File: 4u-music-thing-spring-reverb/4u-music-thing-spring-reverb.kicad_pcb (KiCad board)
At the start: 2 copper layers, 52.8 x 111.5 mm, 52 parts, among them J1 IN1, J2 IN2, J4 OUT, J5 Conn_01x04_Male, J7 CTRL_BOARD_HEADER, J8 MAIN_BOARD_HEADER, U1 TL072, U2 NE5532

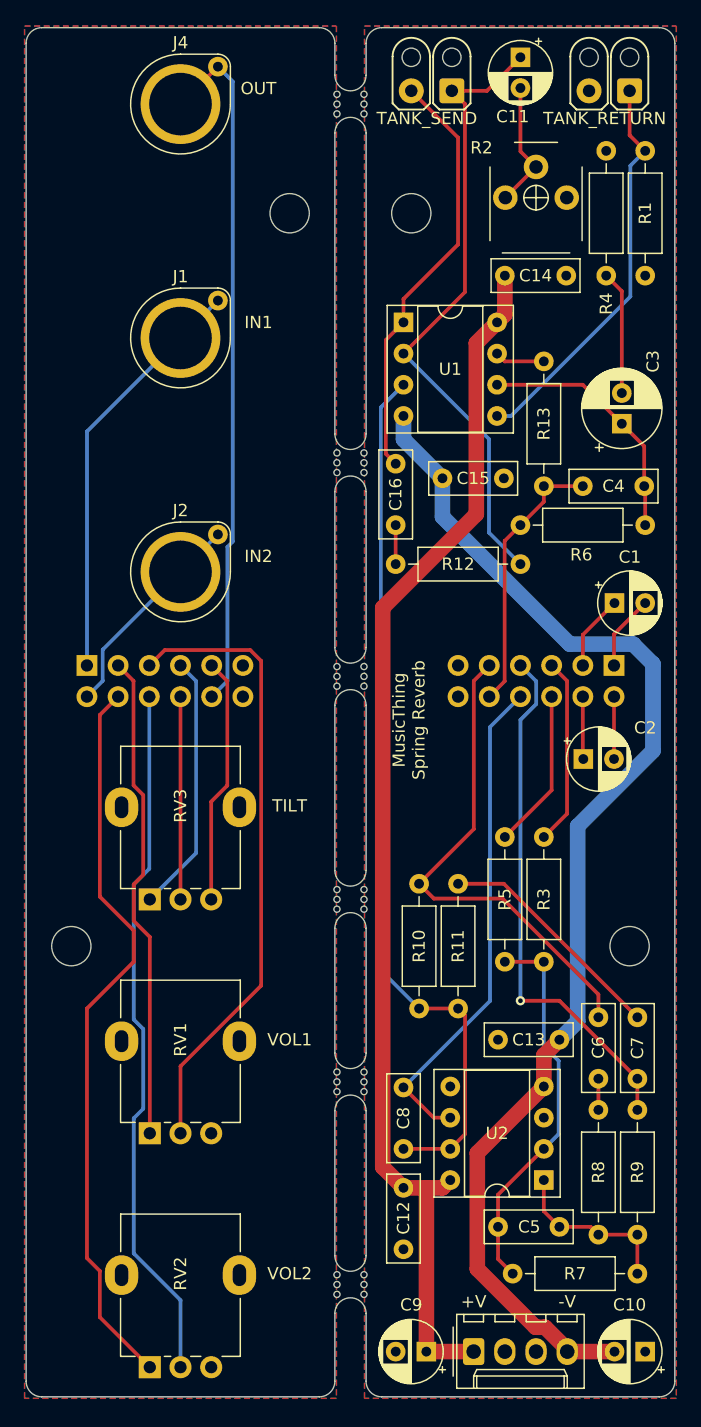
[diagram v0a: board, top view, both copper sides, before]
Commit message: Updated version of music thing spring reverb
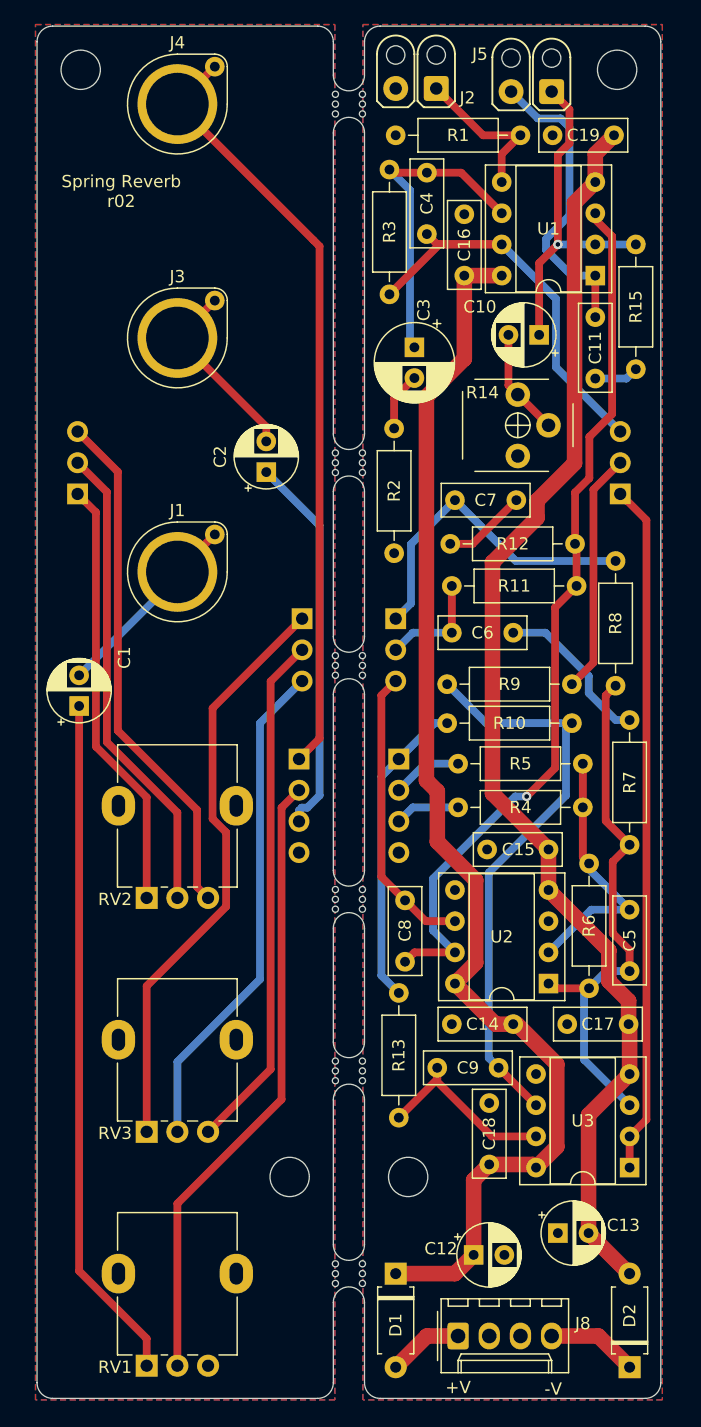
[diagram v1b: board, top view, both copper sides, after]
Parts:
- removed the REF** at (120.9, 53.3)
- removed the REF** at (130.8, 53.3)
- removed the REF** at (148.6, 113.0)
- removed the REF** at (103.1, 113.0)
- removed TANK_RETURN: REV_RETURN, rumblesan-footprints:SolderWire-24AWG-0.2sqmm_1x02_D0.5mm_OD1.1mm_Relief
- removed TANK_SEND: REV_SEND, rumblesan-footprints:SolderWire-24AWG-0.2sqmm_1x02_D0.5mm_OD1.1mm_Relief
- added C17: 100nf, Capacitor_THT:C_Rect_L7.0mm_W2.5mm_P5.00mm, F.Cu at (143.5, 119.4)
- added C18: 100nf, Capacitor_THT:C_Rect_L7.0mm_W2.5mm_P5.00mm, F.Cu at (137.2, 130.8)
- added C19: 100nf, Capacitor_THT:C_Rect_L7.0mm_W2.5mm_P5.00mm, F.Cu at (142.3, 47.0)
- added D1: D, rumblesan-footprints:Diode_THT_P7.62mm_Horizontal, F.Cu at (129.5, 139.7)
- added D2: D, rumblesan-footprints:Diode_THT_P7.62mm_Horizontal, F.Cu at (148.6, 147.3)
- added J10: MIX_MAIN, Connector_PinSocket_2.54mm:PinSocket_1x03_P2.54mm_Vertical, B.Cu at (147.8, 76.2)
- added J11: AUDIO_IO_MAIN, Connector_PinSocket_2.54mm:PinSocket_1x04_P2.54mm_Vertical, B.Cu at (129.8, 97.8)
- added J12: AUDIO_IO_CTRL, Connector_PinHeader_2.54mm:PinHeader_1x04_P2.54mm_Vertical, B.Cu at (121.7, 97.8)
- added J3: IN2, rumblesan-footprints:BananaJack_THT_JohnsonCinch_108-09, F.Cu at (111.8, 63.5)
- added J6: TILT_MAIN, Connector_PinSocket_2.54mm:PinSocket_1x03_P2.54mm_Vertical, B.Cu at (129.5, 86.4)
- added J9: MIX_CTRL, Connector_PinHeader_2.54mm:PinHeader_1x03_P2.54mm_Vertical, B.Cu at (103.6, 76.2)
- added R14: 10k, rumblesan-footprints:Potentiometer_THT_Bourns_3306P_Vertical, F.Cu at (139.5, 70.6)
- added R15: 2k2, rumblesan-footprints:Resistor_THT_L6.3mm_D2.5mm_P10.16mm_Horizontal, F.Cu at (149.1, 66.0)
- added REF**: MountingHole_3.2mm_M3, MountingHole:MountingHole_3.2mm_M3, F.Cu at (103.9, 41.7)
- added REF**: MountingHole_3.2mm_M3, MountingHole:MountingHole_3.2mm_M3, F.Cu at (130.6, 131.8)
- added REF**: MountingHole_3.2mm_M3, MountingHole:MountingHole_3.2mm_M3, F.Cu at (120.9, 131.8)
- added REF**: MountingHole_3.2mm_M3, MountingHole:MountingHole_3.2mm_M3, F.Cu at (147.6, 41.7)
- added U3: TL072, Package_DIP:DIP-8_W7.62mm_Socket, F.Cu at (148.6, 131.1)
- C11: value 10uf -> 10nf; footprint Capacitor_THT:CP_Radial_D5.0mm_P2.50mm -> Capacitor_THT:C_Rect_L7.0mm_W2.5mm_P5.00mm
- C12, C13: value 100nf -> 10uf; footprint Capacitor_THT:C_Rect_L7.0mm_W2.5mm_P5.00mm -> Capacitor_THT:CP_Radial_D5.0mm_P2.50mm
- C16: value 10nf -> 100nf
- C9: value 10uf -> 22pf; footprint Capacitor_THT:CP_Radial_D5.0mm_P2.50mm -> Capacitor_THT:C_Rect_L7.0mm_W2.5mm_P5.00mm
- J2: value IN2 -> REV_RETURN; footprint rumblesan-footprints:BananaJack_THT_JohnsonCinch_108-09 -> rumblesan-footprints:SolderWire-24AWG-0.2sqmm_1x02_D0.5mm_OD1.1mm_Relief
- J5: value Conn_01x04_Male -> REV_SEND; footprint rumblesan-footprints:Molex_KK-254_AE-6410-04A_1x04_P2.54mm_Vertical -> rumblesan-footprints:SolderWire-24AWG-0.2sqmm_1x02_D0.5mm_OD1.1mm_Relief
- J7: value CTRL_BOARD_HEADER -> TILT_CTRL; footprint Connector_PinHeader_2.54mm:PinHeader_2x06_P2.54mm_Vertical -> Connector_PinHeader_2.54mm:PinHeader_1x03_P2.54mm_Vertical
- J8: value MAIN_BOARD_HEADER -> Conn_01x04_Male; footprint Connector_PinSocket_2.54mm:PinSocket_2x06_P2.54mm_Vertical -> rumblesan-footprints:Molex_KK-254_AE-6410-04A_1x04_P2.54mm_Vertical; moved to F.Cu
- R10, R9: value 6k8 -> 100k
- R11, R8: value 2k2 -> 6k8
- R13: value 1k -> 330
- R2: value 10k -> 22r; footprint rumblesan-footprints:Potentiometer_THT_Bourns_3306P_Vertical -> rumblesan-footprints:Resistor_THT_L6.3mm_D2.5mm_P10.16mm_Horizontal
- R3: value 10k -> 22k
- R4: value 22r -> 10k
- R6: value 22k -> 10k
- R7: value 10k -> 2k2
- moved J5 102.8 mm to (142.2, 43.4), turned to 180 degrees
- moved C10 83.3 mm to (141.2, 63.2)
- moved C14 61.0 mm to (139.1, 119.4), turned to 180 degrees
- moved J8 56.1 mm to (134.6, 144.8), turned to 0 degrees
- moved R3 55.8 mm to (129.0, 59.9)
- moved RV2 45.8 mm to (111.8, 101.6)
- moved R7 45.1 mm to (148.6, 94.6), turned to 270 degrees
- moved R8 44.7 mm to (147.4, 81.7)
- moved J2 44.5 mm to (132.8, 43.2), turned to 180 degrees
- moved C1 44.4 mm to (103.8, 93.5), turned to 90 degrees
- moved R4 43.3 mm to (144.8, 101.7), turned to 180 degrees
- moved C7 43.3 mm to (139.4, 76.7), turned to 180 degrees
- moved R13 42.9 mm to (129.8, 116.8), turned to 270 degrees
- moved R6 38.1 mm to (145.3, 116.5), turned to 90 degrees
- moved R9 38.0 mm to (133.7, 91.7), turned to 0 degrees
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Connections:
- C1 pad 1: /AUDIO1_VOL_MAIN -> Net-(C1-Pad1)
- C1 pad 2: /AUDIO1_IN_MAIN -> Net-(C1-Pad2)
- C10 pad 1: GND -> Net-(C10-Pad1)
- C10 pad 2: -12V -> Net-(C10-Pad2)
- C16 pad 1: Net-(C16-Pad1) -> +12V
- C16 pad 2: Net-(C16-Pad2) -> GND
- C2 pad 1: /AUDIO2_VOL_MAIN -> /AUDIO2_IN_CTRL
- C2 pad 2: /AUDIO2_IN_MAIN -> Net-(C2-Pad2)
- C4 pad 1: /AUDIO_OUT_MAIN -> /AUDIO_WET_MAIN
- C5 pad 1: Net-(C5-Pad1) -> /AUDIO_MIX
- C9 pad 1: +12V -> Net-(C9-Pad1)
- C9 pad 2: GND -> Net-(C9-Pad2)
- J1 pad 1: /AUDIO1_IN_CTRL -> Net-(C1-Pad2)
- J2 pad 1: /AUDIO2_IN_CTRL -> Net-(J2-Pad1)
- J5 pad 1: +12V -> Net-(C10-Pad1)
- J5 pad 2: GND -> Net-(C11-Pad1)
- J7 pad 1: /AUDIO1_IN_CTRL -> /TILT_LO_CTRL
- J7 pad 2: /AUDIO2_IN_CTRL -> /TILT_HI_CTRL
- J7 pad 3: /AUDIO1_VOL_CTRL -> /TILT_CENTRE_CTRL
- J8 pad 1: /AUDIO1_IN_MAIN -> Net-(D1-Pad2)
- J8 pad 2: /AUDIO2_IN_MAIN -> GND
- J8 pad 3: /AUDIO1_VOL_MAIN -> GND
- J8 pad 4: /AUDIO2_VOL_MAIN -> Net-(D2-Pad1)
- R1 pad 1: Net-(J3-Pad1) -> Net-(J2-Pad1)
- R10 pad 1: Net-(C8-Pad1) -> /AUDIO_OUT_MAIN
- R10 pad 2: /TILT_HI_MAIN -> Net-(C9-Pad2)
- R11 pad 2: Net-(C7-Pad1) -> /TILT_HI_MAIN
- R12 pad 1: Net-(C16-Pad2) -> Net-(C8-Pad1)
- R12 pad 2: Net-(C11-Pad1) -> Net-(C7-Pad1)
- R13 pad 2: Net-(R13-Pad2) -> Net-(C9-Pad1)
- R2 pad 1: Net-(C11-Pad2) -> Net-(C3-Pad2)
- R2 pad 2: Net-(C11-Pad2) -> GND
- R3 pad 1: Net-(C5-Pad2) -> /AUDIO_WET_MAIN
- R3 pad 2: /AUDIO1_POST_VOL_MAIN -> Net-(C3-Pad1)
- R4 pad 1: Net-(C3-Pad2) -> Net-(C5-Pad2)
- R4 pad 2: GND -> /AUDIO2_IN_MAIN
- R5 pad 2: /AUDIO2_POST_VOL_MAIN -> /AUDIO1_IN_MAIN
- R6 pad 1: /AUDIO_OUT_MAIN -> /AUDIO_MIX
- R6 pad 2: Net-(C3-Pad1) -> Net-(C5-Pad2)
- R7 pad 1: Net-(C5-Pad1) -> Net-(C6-Pad2)
- R7 pad 2: Net-(C5-Pad2) -> /AUDIO_MIX
- R8 pad 1: Net-(C6-Pad2) -> /TILT_LO_MAIN
- R8 pad 2: Net-(C5-Pad1) -> /AUDIO_MIX
- R9 pad 1: /TILT_LO_MAIN -> Net-(C9-Pad2)
- R9 pad 2: Net-(C5-Pad1) -> /AUDIO_MIX_MAIN
- RV1 pad 1: /AUDIO1_VOL_CTRL -> Net-(C1-Pad1)
- RV1 pad 2: /AUDIO1_POST_VOL_CTRL -> /AUDIO1_IN_CTRL
- RV2 pad 1: /AUDIO2_VOL_CTRL -> /AUDIO_DRY_CTRL
- RV2 pad 2: /AUDIO2_POST_VOL_CTRL -> /AUDIO_MIX_CTRL
- RV2 pad 3: GND1 -> /AUDIO_WET_CTRL
- U1 pad 1: Net-(C16-Pad1) -> Net-(C11-Pad1)
- U1 pad 2: Net-(C11-Pad1) -> Net-(C10-Pad1)
- U1 pad 5: Net-(J3-Pad1) -> Net-(J2-Pad1)
- U1 pad 7: Net-(R13-Pad2) -> /AUDIO_WET_MAIN
- U2 pad 1: Net-(C5-Pad1) -> /AUDIO_MIX
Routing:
- net /AUDIO2_VOL_CTRL: track 60.1 -> 0.00 mm
- net /AUDIO2_POST_VOL_CTRL: track 57.4 -> 0.00 mm
- net /AUDIO_DRY_MAIN: track 0.00 -> 56.3 mm
- net Net-(C1-Pad1): track 0.00 -> 56.0 mm
- net /AUDIO1_POST_VOL_CTRL: track 51.2 -> 0.00 mm
- net Net-(C9-Pad2): track 0.00 -> 47.0 mm
- net /AUDIO_MIX: track 0.00 -> 44.1 mm
- net /AUDIO_WET_CTRL: track 0.00 -> 42.4 mm
- net /AUDIO1_VOL_CTRL: track 40.6 -> 0.00 mm
- net /AUDIO_MIX_CTRL: track 0.00 -> 38.8 mm
- net /AUDIO_WET_MAIN: track 0.00 -> 36.5 mm
- net /AUDIO_DRY_CTRL: track 0.00 -> 35.2 mm
- net Net-(C16-Pad1): track 34.7 -> 0.00 mm
- net Net-(J3-Pad1): track 32.7 -> 0.00 mm
- net /TILT_HI_MAIN: track 40.3 -> 8.96 mm
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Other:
- board size 52.8 x 111.5 mm -> 50.8 x 111.8 mm
- board text added: "RETURN"
- board text added: "S"
- board text added: "SEND"
- board text added: "Spring Reverb r02"
- board text added: "T"
- board text removed: "IN1"
- board text removed: "IN2"
- board text removed: "MusicThing Spring Reverb"
- board text removed: "OUT"
- board text removed: "TILT"
- board text removed: "VOL1"
- board text removed: "VOL2"

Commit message: Updating spring reverb to rev3
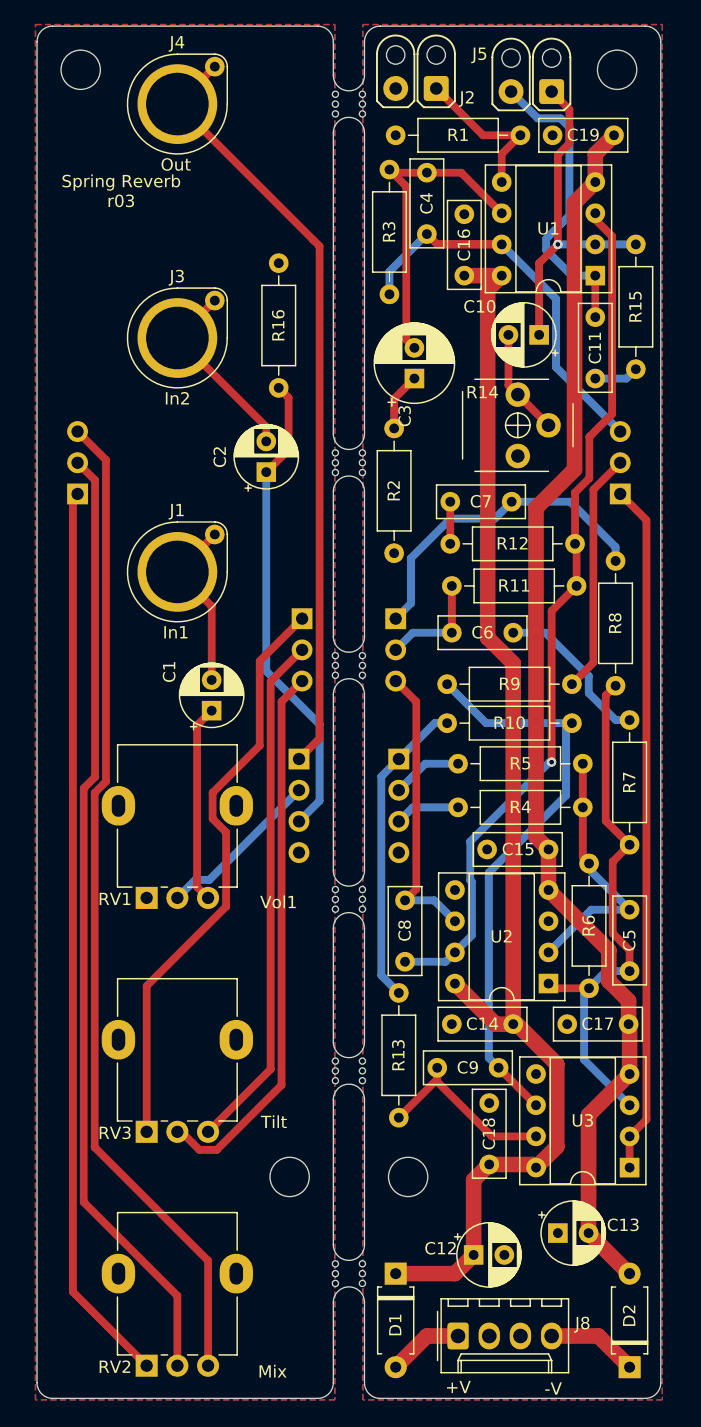
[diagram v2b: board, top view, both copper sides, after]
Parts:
- added R16: 100k, rumblesan-footprints:Resistor_THT_L6.3mm_D2.5mm_P10.16mm_Horizontal, F.Cu at (120.0, 67.6)
- C11: value 10nf -> 3n3f
- D1, D2: value D -> 1n4004
- moved RV1 38.1 mm to (111.8, 101.6)
- moved RV2 38.1 mm to (111.8, 139.7)
- moved C1 10.8 mm to (114.6, 93.9)
- moved C7 5.38 mm to (134.0, 76.8), turned to 0 degrees
- moved C3 2.54 mm to (131.1, 66.8), turned to 90 degrees
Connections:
- C4 pad 2: Net-(C3-Pad1) -> Net-(C3-Pad2)
- R2 pad 1: Net-(C3-Pad2) -> Net-(C3-Pad1)
- R3 pad 2: Net-(C3-Pad1) -> Net-(C3-Pad2)
- RV1 pad 1: Net-(C1-Pad1) -> GND1
- RV1 pad 3: GND1 -> Net-(C1-Pad1)
- U1 pad 6: Net-(C3-Pad1) -> Net-(C3-Pad2)
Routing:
- net Net-(C1-Pad1): track 56.0 -> 16.1 mm
- net /AUDIO_MIX_CTRL: track 38.8 -> 77.7 mm
- net /AUDIO_WET_CTRL: track 42.4 -> 81.2 mm
- net /AUDIO_DRY_CTRL: track 35.2 -> 73.6 mm
- net /AUDIO1_IN_CTRL: track 51.0 -> 13.5 mm
- net Net-(C3-Pad2): track 4.79 -> 26.0 mm
- net Net-(C3-Pad1): track 25.9 -> 4.75 mm
- net /AUDIO2_IN_CTRL: track 31.2 -> 38.9 mm
- net /TILT_CENTRE_CTRL: track 41.2 -> 45.2 mm
- net Net-(C7-Pad1): track 6.85 -> 3.43 mm
- net -12V: track 104.2 -> 101.3 mm
- net Net-(C8-Pad1): track 72.6 -> 70.8 mm
- net +12V: track 103.3 -> 104.3 mm
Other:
- board text added: "In1"
- board text added: "In2"
- board text added: "Mix"
- board text added: "Out"
- board text added: "Spring Reverb r03"
- board text added: "Tilt"
- board text added: "Vol1"
- board text removed: "Spring Reverb r02"
